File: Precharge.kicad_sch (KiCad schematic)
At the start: 4 parts

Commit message: more schematic work and initial layout
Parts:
- removed D2: LED_RGB, LED_SMD:LED_RGB_5050-6, symbol Device:LED_RGB
- removed R6, R7: 50, Resistor_SMD:R_0603_1608Metric_Pad0.98x0.95mm_HandSolder, symbol Device:R
- removed R8: 120, Resistor_SMD:R_0603_1608Metric_Pad0.98x0.95mm_HandSolder, symbol Device:R
- added R30: 33, Resistor_SMD:R_2512_6332Metric, symbol Device:R
- added R31: 470, Resistor_SMD:R_0603_1608Metric_Pad0.98x0.95mm_HandSolder, symbol Device:R
- added U7: TLP175A, Package_SO:Toshiba_SOIC-4-6_4.4x3.6mm_P1.27mm, symbol Relay_SolidState:TLP175A
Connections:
- net GND: now also U7.3
- new net: R30.1, U7.4
- new net: R31.2, U7.1
- new net ENABLE: R31.1
- new net SW1: U7.6
- new net SW2: R30.2

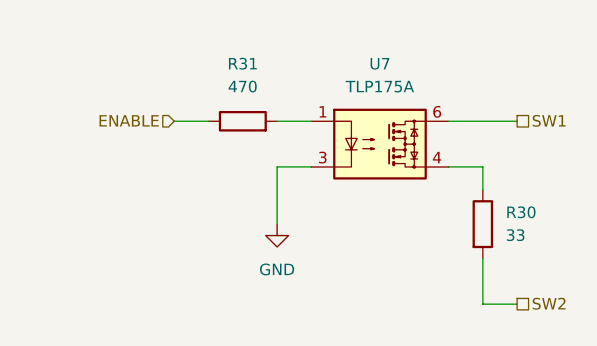
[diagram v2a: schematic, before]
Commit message: schematic changes and initial routing
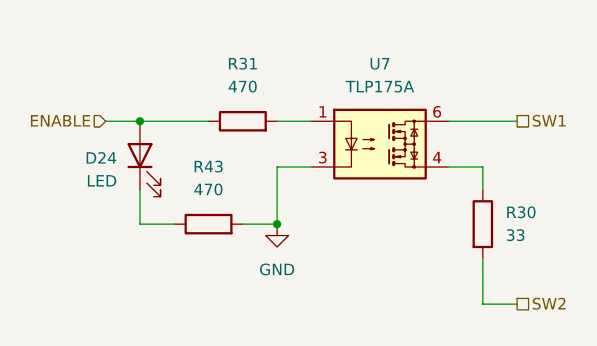
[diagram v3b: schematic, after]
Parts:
- added D24: LED, LED_SMD:LED_0603_1608Metric_Pad1.05x0.95mm_HandSolder, symbol Device:LED
- added R43: 470, Resistor_SMD:R_0603_1608Metric_Pad0.98x0.95mm_HandSolder, symbol Device:R
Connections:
- net ENABLE: now also D24.2 (A)
- net GND: now also R43.2
- new net: D24.1 (K), R43.1
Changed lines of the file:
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@@
 	(generator_version "10.0")
 	(paper "A4")
+	(junction
+		(at 101.6 86.36)
+		(diameter 0)
+		(color 0 0 0 0)
+	)
+	(junction
+		(at 116.84 97.79)
+		(diameter 0)
+		(color 0 0 0 0)
+	)
+	(wire
+		(pts
+			(xy 105.41 97.79) (xy 101.6 97.79)
+		)
+		(stroke
+			(width 0)
+			(type default)
+		)
+	)
 	(wire
 		(pts
@@
 	(wire
 		(pts
-			(xy 105.41 86.36) (xy 109.22 86.36)
+			(xy 97.79 86.36) (xy 101.6 86.36)
 		)
 		(stroke
@@
 	(wire
 		(pts
+			(xy 113.03 97.79) (xy 116.84 97.79)
+		)
+		(stroke
+			(width 0)
+			(type default)
+		)
+	)
+	(wire
+		(pts
+			(xy 101.6 93.98) (xy 101.6 97.79)
+		)
+		(stroke
+			(width 0)
+			(type default)
+		)
+	)
+	(wire
+		(pts
 			(xy 135.89 91.44) (xy 139.7 91.44)
 		)
@@
 		(pts
 			(xy 139.7 101.6) (xy 139.7 106.68)
+		)
+		(stroke
+			(width 0)
+			(type default)
+		)
+	)
+	(wire
+		(pts
+			(xy 101.6 86.36) (xy 109.22 86.36)
 		)
 		(stroke
@@
 	(hierarchical_label "ENABLE"
 		(shape input)
-		(at 105.41 86.36 180)
+		(at 97.79 86.36 180)
 		(effects
 			(font
@@
 	)
 	(symbol
+		(lib_id "Device:R")
+		(at 109.22 97.79 90)
+		(unit 1)
+		(body_style 1)
+		(exclude_from_sim no)
+		(in_bom yes)
+		(on_board yes)
+		(in_pos_files yes)
+		(dnp no)
+		(fields_autoplaced yes)
+		(property "Reference" "R43"
+			(at 109.22 91.44 90)
+			(show_name no)
+			(do_not_autoplace no)
+			(effects
+				(font
+					(size 1.27 1.27)
+				)
+			)
+		)
+		(property "Value" "470"
+			(at 109.22 93.98 90)
+			(show_name no)
+			(do_not_autoplace no)
+			(effects
+				(font
+					(size 1.27 1.27)
+				)
+			)
+		)
+		(property "Footprint" "Resistor_SMD:R_0603_1608Metric_Pad0.98x0.95mm_HandSolder"
+			(at 109.22 99.568 90)
+			(hide yes)
+			(show_name no)
+			(do_not_autoplace no)
+			(effects
+				(font
+					(size 1.27 1.27)
+				)
+			)
+		)
+		(property "Datasheet" ""
+			(at 109.22 97.79 0)
+			(hide yes)
+			(show_name no)
+			(do_not_autoplace no)
+			(effects
+				(font
+					(size 1.27 1.27)
+				)
+			)
+		)
+		(property "Description" "Resistor"
+			(at 109.22 97.79 0)
+			(hide yes)
+			(show_name no)
+			(do_not_autoplace no)
+			(effects
+				(font
+					(size 1.27 1.27)
+				)
+			)
+		)
+		(pin "1"
+		)
+		(pin "2"
+		)
+		(instances
+			(project "RSC-LV3-LVBPS"
+				(path "/4bbf2fff-9f66-421d-84bf-68d1dcd1e11d/9a0a496f-39db-441a-9686-17b43a03a46f"
+					(reference "R43")
+					(unit 1)
+				)
+			)
+		)
+	)
+	(symbol
 		(lib_id "power:GND")
 		(at 116.84 97.79 0)
@@
 					(unit 1)
 				)
+			)
+		)
+	)
+	(symbol
+		(lib_id "Device:LED")
+		(at 101.6 90.17 90)
+		(unit 1)
+		(body_style 1)
+		(exclude_from_sim no)
+		(in_bom yes)
+		(on_board yes)
+		(in_pos_files yes)
+		(dnp no)
+		(fields_autoplaced yes)
+		(property "Reference" "D24"
+			(at 99.06 90.4874 90)
+			(show_name no)
+			(do_not_autoplace no)
+			(effects
+				(font
+					(size 1.27 1.27)
+				)
+				(justify left)
+			)
+		)
+		(property "Value" "LED"
+			(at 99.06 93.0274 90)
+			(show_name no)
+			(do_not_autoplace no)
+			(effects
+				(font
+					(size 1.27 1.27)
+				)
+				(justify left)
+			)
+		)
+		(property "Footprint" "LED_SMD:LED_0603_1608Metric_Pad1.05x0.95mm_HandSolder"
+			(at 101.6 90.17 0)
+			(hide yes)
+			(show_name no)
+			(do_not_autoplace no)
+			(effects
+				(font
+					(size 1.27 1.27)
+				)
+			)
+		)
+		(property "Datasheet" ""
+			(at 101.6 90.17 0)
+			(hide yes)
+			(show_name no)
+			(do_not_autoplace no)
+			(effects
+				(font
+					(size 1.27 1.27)
+				)
+			)
+		)
+		(property "Description" "Light emitting diode"
+			(at 101.6 90.17 0)
+			(hide yes)
+			(show_name no)
+			(do_not_autoplace no)
+			(effects
+				(font
+					(size 1.27 1.27)
+				)
+			)
+		)
+		(property "Sim.Pins" "1=K 2=A"
+			(at 101.6 90.17 0)
+			(hide yes)
+			(show_name no)
+			(do_not_autoplace no)
+			(effects
+				(font
+					(size 1.27 1.27)
+				)
+			)
+		)
+		(pin "1"
+		)
+		(pin "2"
+		)
+		(instances
+			(project "RSC-LV3-LVBPS"
+				(path "/4bbf2fff-9f66-421d-84bf-68d1dcd1e11d/9a0a496f-39db-441a-9686-17b43a03a46f"
+					(reference "D24")
+					(unit 1)
+				)

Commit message: finished layout, routing, and silkscreen
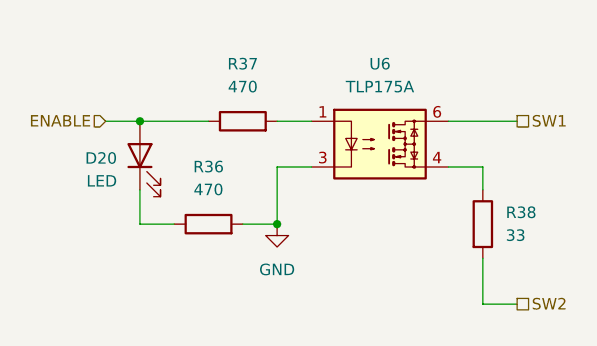
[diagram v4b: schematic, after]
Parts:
- renumbered D24 to D20, R43 to R36, R31 to R37, R30 to R38, U7 to U6
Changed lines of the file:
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@@
 		(dnp no)
 		(fields_autoplaced yes)
-		(property "Reference" "R30"
+		(property "Reference" "R38"
 			(at 142.24 96.5199 0)
 			(show_name no)
@@
 			(project "RSC-LV3-LVBPS"
 				(path "/4bbf2fff-9f66-421d-84bf-68d1dcd1e11d/9a0a496f-39db-441a-9686-17b43a03a46f"
-					(reference "R30")
+					(reference "R38")
 					(unit 1)
 				)
@@
 		(dnp no)
 		(fields_autoplaced yes)
-		(property "Reference" "R43"
+		(property "Reference" "R36"
 			(at 109.22 91.44 90)
 			(show_name no)
@@
 			(project "RSC-LV3-LVBPS"
 				(path "/4bbf2fff-9f66-421d-84bf-68d1dcd1e11d/9a0a496f-39db-441a-9686-17b43a03a46f"
-					(reference "R43")
+					(reference "R36")
 					(unit 1)
 				)
@@
 		(dnp no)
 		(fields_autoplaced yes)
-		(property "Reference" "#PWR064"
+		(property "Reference" "#PWR066"
 			(at 116.84 104.14 0)
 			(hide yes)
@@
 			(project "RSC-LV3-LVBPS"
 				(path "/4bbf2fff-9f66-421d-84bf-68d1dcd1e11d/9a0a496f-39db-441a-9686-17b43a03a46f"
-					(reference "#PWR064")
+					(reference "#PWR066")
 					(unit 1)
 				)
@@
 		(dnp no)
 		(fields_autoplaced yes)
-		(property "Reference" "U7"
+		(property "Reference" "U6"
 			(at 128.27 80.01 0)
 			(show_name no)
@@
 			(project "RSC-LV3-LVBPS"
 				(path "/4bbf2fff-9f66-421d-84bf-68d1dcd1e11d/9a0a496f-39db-441a-9686-17b43a03a46f"
-					(reference "U7")
+					(reference "U6")
 					(unit 1)
 				)
@@
 		(dnp no)
 		(fields_autoplaced yes)
-		(property "Reference" "R31"
+		(property "Reference" "R37"
 			(at 113.03 80.01 90)
 			(show_name no)
@@
 			(project "RSC-LV3-LVBPS"
 				(path "/4bbf2fff-9f66-421d-84bf-68d1dcd1e11d/9a0a496f-39db-441a-9686-17b43a03a46f"
-					(reference "R31")
+					(reference "R37")
 					(unit 1)
 				)
@@
 		(dnp no)
 		(fields_autoplaced yes)
-		(property "Reference" "D24"
+		(property "Reference" "D20"
 			(at 99.06 90.4874 90)
 			(show_name no)
@@
 			(project "RSC-LV3-LVBPS"
 				(path "/4bbf2fff-9f66-421d-84bf-68d1dcd1e11d/9a0a496f-39db-441a-9686-17b43a03a46f"
-					(reference "D24")
-					(unit 1)
-				)
+					(reference "D20")
+					(unit 1)
+				)

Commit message: r0 final
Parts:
- renumbered D20 to D15
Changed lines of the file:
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@@
 		(dnp no)
 		(fields_autoplaced yes)
-		(property "Reference" "#PWR066"
+		(property "Reference" "#PWR069"
 			(at 116.84 104.14 0)
 			(hide yes)
@@
 			(project "RSC-LV3-LVBPS"
 				(path "/4bbf2fff-9f66-421d-84bf-68d1dcd1e11d/9a0a496f-39db-441a-9686-17b43a03a46f"
-					(reference "#PWR066")
+					(reference "#PWR069")
 					(unit 1)
 				)
@@
 		(dnp no)
 		(fields_autoplaced yes)
-		(property "Reference" "D20"
+		(property "Reference" "D15"
 			(at 99.06 90.4874 90)
 			(show_name no)
@@
 			(project "RSC-LV3-LVBPS"
 				(path "/4bbf2fff-9f66-421d-84bf-68d1dcd1e11d/9a0a496f-39db-441a-9686-17b43a03a46f"
-					(reference "D20")
+					(reference "D15")
 					(unit 1)
 				)
